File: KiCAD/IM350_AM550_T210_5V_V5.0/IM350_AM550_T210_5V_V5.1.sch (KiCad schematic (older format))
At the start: 32 parts, among them J1 USB_B_Micro_Power, J2 RJ12, Q1 BC847, SW1 SW_Push, U1 AMS1117-3.3, U2 ESP-12F, U3 TSS721ADR, U4 EL357NC, U5 EL357NC

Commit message: Update
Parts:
- removed R13: 0, Resistor_SMD:R_0201_0603Metric_Pad0.64x0.40mm_HandSolder, symbol Device:R
- added D1: 1N4148WS, Diode_SMD:D_SOD-323_HandSoldering, symbol Diode:1N4148WS
- U3: symbol TSS721ADR:TSS721ADR -> IM350_AM550_T210_5V_V5.0-rescue:TSS721ADR-TSS721ADR
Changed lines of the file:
@@
 NoConn ~ 1150 5400
 $Comp
-L TSS721ADR:TSS721ADR U3
+L IM350_AM550_T210_5V_V5.0-rescue:TSS721ADR-TSS721ADR U3
 U 1 1 61633360
 P 8200 2350
@@
 	8900 1650 9550 1650
 Wire Wire Line
-	7500 950  9550 950
-Wire Wire Line
 	2800 4600 2800 4650
 $Comp
@@
 Wire Wire Line
 	10250 2150 10250 2500
-$Comp
-L Device:R R13
-U 1 1 616AFA1A
-P 10150 2350
-F 0 "R13" V 10100 2500 50  0000 C CNN
-F 1 "0" V 10150 2350 50  0000 C CNN
-F 2 "Resistor_SMD:R_0201_0603Metric_Pad0.64x0.40mm_HandSolder" V 10080 2350 50  0001 C CNN
-F 3 "~" H 10150 2350 50  0001 C CNN
-	1    10150 2350
-	-1   0    0    1
-$EndComp
 Connection ~ 10250 2500
 Wire Wire Line
@@
 Text Label 2650 4400 0    50   ~ 0
 MBUS_RX
+$Comp
+L Diode:1N4148WS D1
+U 1 1 61830095
+P 10150 2350
+F 0 "D1" V 10250 2250 50  0000 L CNN
+F 1 "1N4148WS" V 10350 2150 50  0000 L CNN
+F 2 "Diode_SMD:D_SOD-323_HandSoldering" H 10150 2175 50  0001 C CNN
+F 3 "https://www.vishay.com/docs/85751/1n4148ws.pdf" H 10150 2350 50  0001 C CNN
+	1    10150 2350
+	0    1    1    0
+$EndComp
+Wire Wire Line
+	7500 950  9550 950
 $EndSCHEMATC

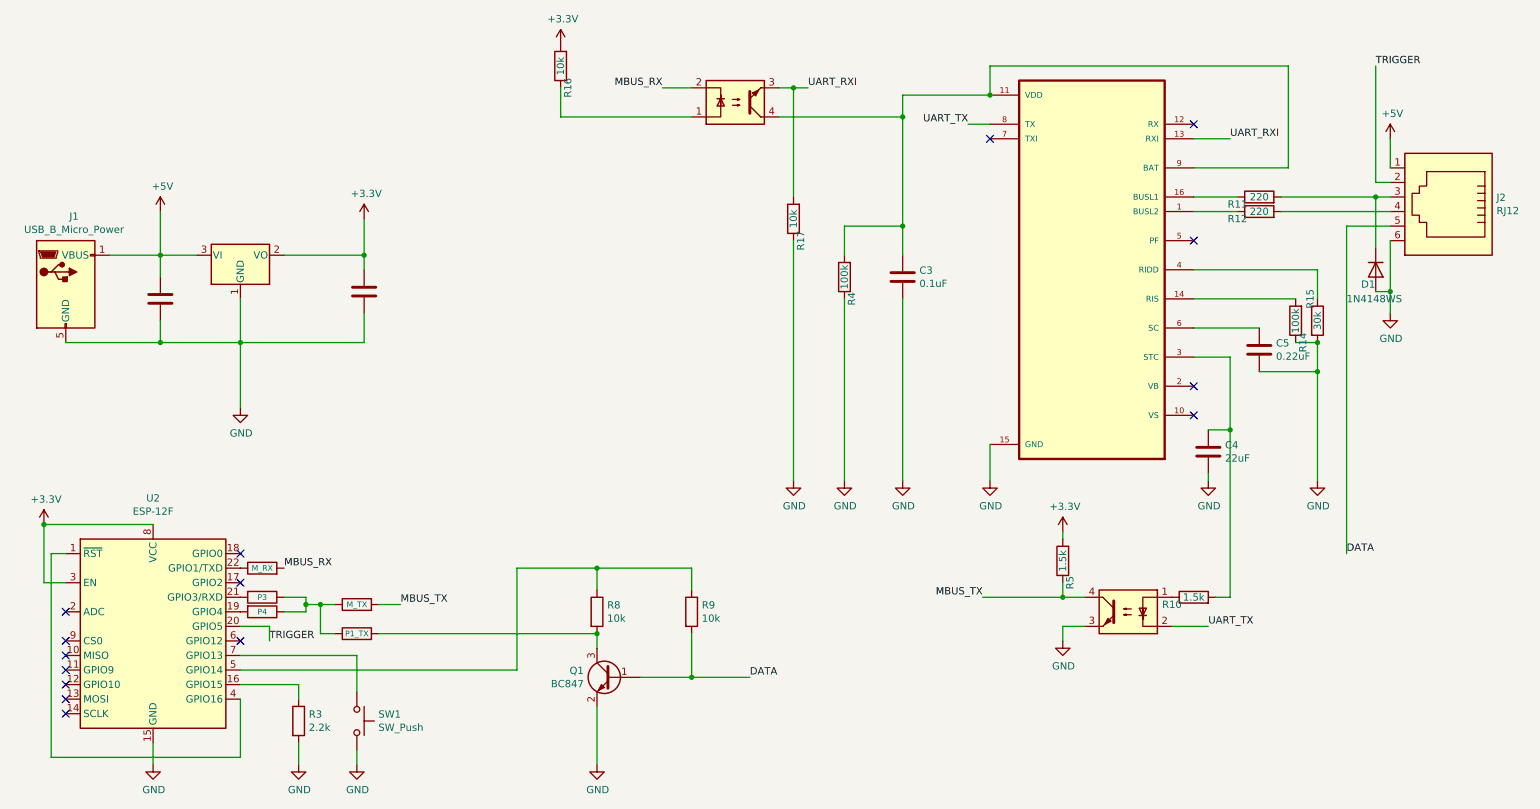
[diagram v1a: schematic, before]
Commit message: MBus for Smartmeter added
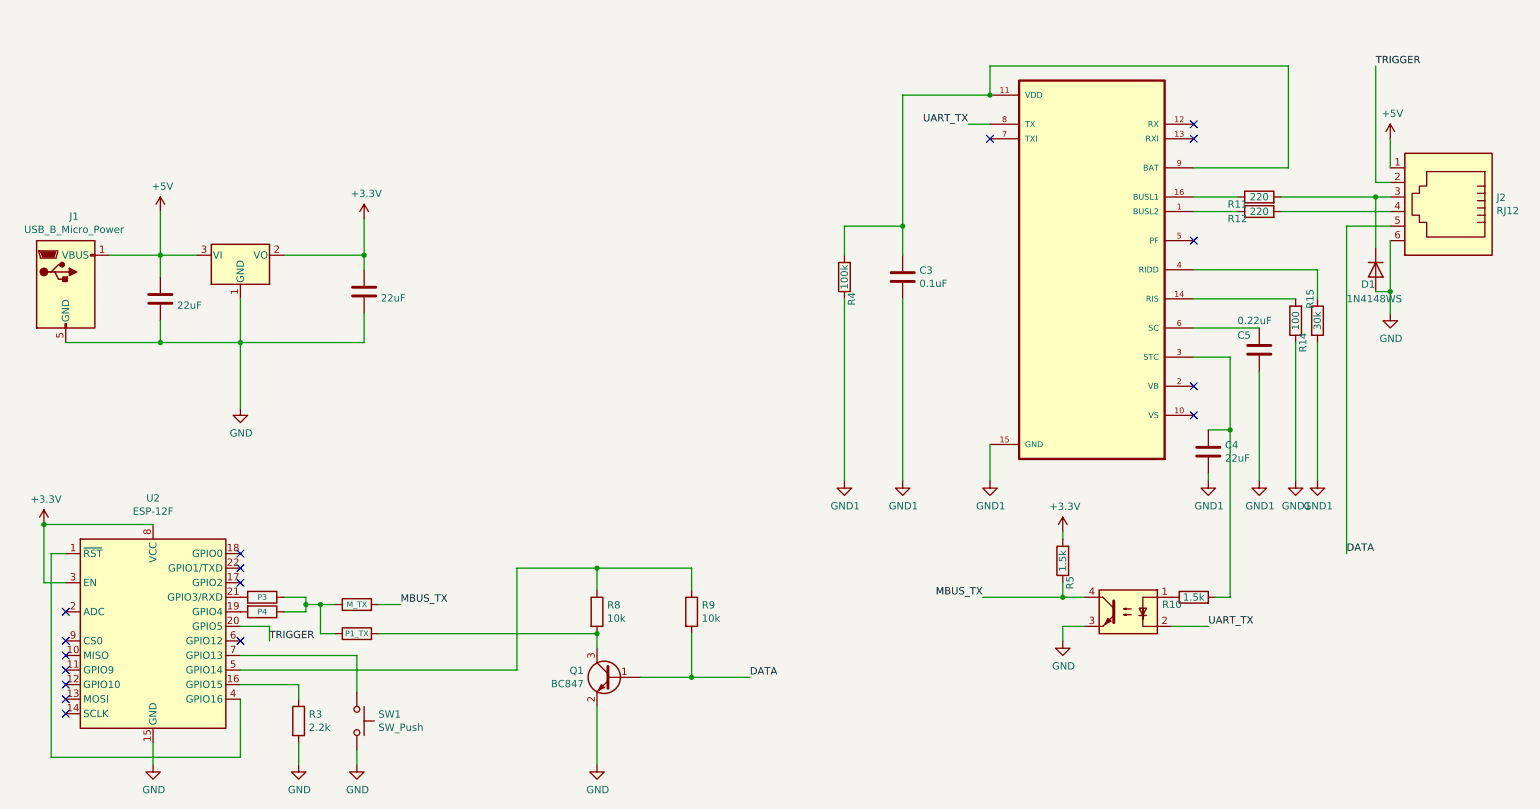
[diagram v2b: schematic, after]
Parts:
- removed R16, R17: 10k, Resistor_SMD:R_0805_2012Metric_Pad1.20x1.40mm_HandSolder, symbol Device:R
- removed R18: M_RX, Resistor_SMD:R_0201_0603Metric_Pad0.64x0.40mm_HandSolder, symbol Device:R
- removed U5: EL357NC, Package_SO:SOIC-4_4.55x2.6mm_P1.27mm, symbol Isolator:TLP291
- R1, R2, R6, R7: footprint Resistor_SMD:R_0201_0603Metric_Pad0.64x0.40mm_HandSolder -> Resistor_SMD:R_0603_1608Metric_Pad0.98x0.95mm_HandSolder
- R14: value 100k -> 100
- U4: footprint Package_SO:SOIC-4_4.55x2.6mm_P1.27mm -> Package_SO:SOP-4_3.8x4.1mm_P2.54mm
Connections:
- net GND: no longer C3.2, C4.2, C5.2, R14.1, R15.2, R4.1, U3.15 (GND)
- net UART_RXI: no longer names the net of U3.13 (RXI)
- new net GND1: C3.2, C4.2, C5.2, R14.1, R15.2, R4.1, U3.15 (GND)
- no-connect marks 15 -> 17
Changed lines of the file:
@@
 P 3200 2500
 F 0 "C1" H 3315 2546 50  0001 L CNN
-F 1 "22uF" H 3315 2455 50  0001 L CNN
+F 1 "22uF" H 3315 2455 50  0000 L CNN
 F 2 "Capacitor_SMD:C_1206_3216Metric_Pad1.33x1.80mm_HandSolder" H 3238 2350 50  0001 C CNN
 F 3 "~" H 3200 2500 50  0001 C CNN
@@
 F 0 "R1" V 2450 4750 50  0001 C CNN
 F 1 "P3" V 2500 4600 39  0000 C CNN
-F 2 "Resistor_SMD:R_0201_0603Metric_Pad0.64x0.40mm_HandSolder" V 2430 4600 50  0001 C CNN
+F 2 "Resistor_SMD:R_0603_1608Metric_Pad0.98x0.95mm_HandSolder" V 2430 4600 50  0001 C CNN
 F 3 "~" H 2500 4600 50  0001 C CNN
 	1    2500 4600
@@
 F 0 "R2" V 2550 4850 50  0001 C CNN
 F 1 "P4" V 2500 4700 39  0000 C CNN
-F 2 "Resistor_SMD:R_0201_0603Metric_Pad0.64x0.40mm_HandSolder" V 2430 4700 50  0001 C CNN
+F 2 "Resistor_SMD:R_0603_1608Metric_Pad0.98x0.95mm_HandSolder" V 2430 4700 50  0001 C CNN
 F 3 "~" H 2500 4700 50  0001 C CNN
 	1    2500 4700
@@
 Wire Wire Line
 	7500 3800 7500 3550
-$Comp
-L power:GND #PWR0102
-U 1 1 6164BD9D
-P 7500 3800
-F 0 "#PWR0102" H 7500 3550 50  0001 C CNN
-F 1 "GND" H 7505 3627 50  0000 C CNN
-F 2 "" H 7500 3800 50  0001 C CNN
-F 3 "" H 7500 3800 50  0001 C CNN
-	1    7500 3800
-	1    0    0    -1
-$EndComp
 NoConn ~ 7500 1450
 NoConn ~ 8900 2150
@@
 P 1800 2550
 F 0 "C2" H 1915 2596 50  0001 L CNN
-F 1 "22uF" H 1915 2505 50  0001 L CNN
+F 1 "22uF" H 1915 2505 50  0000 L CNN
 F 2 "Capacitor_SMD:C_1206_3216Metric_Pad1.33x1.80mm_HandSolder" H 1838 2400 50  0001 C CNN
 F 3 "~" H 1800 2550 50  0001 C CNN
@@
 F 0 "R6" V 3100 4800 50  0001 C CNN
 F 1 "M_TX" V 3150 4650 39  0000 C CNN
-F 2 "Resistor_SMD:R_0201_0603Metric_Pad0.64x0.40mm_HandSolder" V 3080 4650 50  0001 C CNN
+F 2 "Resistor_SMD:R_0603_1608Metric_Pad0.98x0.95mm_HandSolder" V 3080 4650 50  0001 C CNN
 F 3 "~" H 3150 4650 50  0001 C CNN
 	1    3150 4650
@@
 F 0 "R7" V 3100 5000 50  0001 C CNN
 F 1 "P1_TX" V 3150 4850 39  0000 C CNN
-F 2 "Resistor_SMD:R_0201_0603Metric_Pad0.64x0.40mm_HandSolder" V 3080 4850 50  0001 C CNN
+F 2 "Resistor_SMD:R_0603_1608Metric_Pad0.98x0.95mm_HandSolder" V 3080 4850 50  0001 C CNN
 F 3 "~" H 3150 4850 50  0001 C CNN
 	1    3150 4850
@@
 F 0 "U4" H 8450 5025 50  0001 C CNN
 F 1 "EL357NC" H 8450 4934 50  0001 C CNN
-F 2 "Package_SO:SOIC-4_4.55x2.6mm_P1.27mm" H 8250 4500 50  0001 L CNN
+F 2 "Package_SO:SOP-4_3.8x4.1mm_P2.54mm" H 8250 4500 50  0001 L CNN
 F 3 "https://toshiba.semicon-storage.com/info/docget.jsp?did=12884&prodName=TLP291" H 8450 4700 50  0001 L CNN
 	1    8450 4700
@@
 Wire Wire Line
 	7500 1150 6900 1150
-Wire Wire Line
-	6900 1150 6900 1300
 Connection ~ 7500 1150
-$Comp
-L power:GND #PWR02
-U 1 1 616F92D3
-P 6900 3800
-F 0 "#PWR02" H 6900 3550 50  0001 C CNN
-F 1 "GND" H 6905 3627 50  0000 C CNN
-F 2 "" H 6900 3800 50  0001 C CNN
-F 3 "" H 6900 3800 50  0001 C CNN
-	1    6900 3800
-	1    0    0    -1
-$EndComp
 Wire Wire Line
 	6900 2550 6900 3800
@@
 Wire Wire Line
 	6900 2050 6900 2250
-$Comp
-L power:GND #PWR01
-U 1 1 616FD0E7
-P 6500 3800
-F 0 "#PWR01" H 6500 3550 50  0001 C CNN
-F 1 "GND" H 6505 3627 50  0000 C CNN
-F 2 "" H 6500 3800 50  0001 C CNN
-F 3 "" H 6500 3800 50  0001 C CNN
-	1    6500 3800
-	1    0    0    -1
-$EndComp
 Wire Wire Line
 	6500 2550 6500 3800
@@
 P 9600 2700
 F 0 "R14" V 9550 2850 50  0000 C CNN
-F 1 "100k" V 9600 2700 50  0000 C CNN
+F 1 "100" V 9600 2700 50  0000 C CNN
 F 2 "Resistor_SMD:R_0805_2012Metric_Pad1.20x1.40mm_HandSolder" V 9530 2700 50  0001 C CNN
 F 3 "~" H 9600 2700 50  0001 C CNN
 	1    9600 2700
 	-1   0    0    1
-$EndComp
-$Comp
-L power:GND #PWR06
-U 1 1 6170140B
-P 9750 3800
-F 0 "#PWR06" H 9750 3550 50  0001 C CNN
-F 1 "GND" H 9755 3627 50  0000 C CNN
-F 2 "" H 9750 3800 50  0001 C CNN
-F 3 "" H 9750 3800 50  0001 C CNN
-	1    9750 3800
-	1    0    0    -1
 $EndComp
 $Comp
@@
 	8900 2950 9150 2950
 Wire Wire Line
-	9750 2850 9750 3050
-Wire Wire Line
 	9000 3450 9150 3450
 Connection ~ 9150 3450
 Wire Wire Line
 	9150 3450 9150 4600
-$Comp
-L power:GND #PWR05
-U 1 1 6173CE86
-P 9000 3800
-F 0 "#PWR05" H 9000 3550 50  0001 C CNN
-F 1 "GND" H 9005 3627 50  0000 C CNN
-F 2 "" H 9000 3800 50  0001 C CNN
-F 3 "" H 9000 3800 50  0001 C CNN
-	1    9000 3800
-	1    0    0    -1
-$EndComp
 Wire Wire Line
 	9000 3750 9000 3800
@@
 	1    0    0    -1
 $EndComp
-Wire Wire Line
-	9600 2850 9750 2850
-Connection ~ 9750 2850
 Wire Wire Line
 	9750 2350 9750 2550
@@
 U 1 1 61763C16
 P 9350 2900
-F 0 "C5" H 9465 2946 50  0000 L CNN
-F 1 "0.22uF" H 9465 2855 50  0000 L CNN
+F 0 "C5" H 9200 3000 50  0000 L CNN
+F 1 "0.22uF" H 9200 3100 50  0000 L CNN
 F 2 "Capacitor_SMD:C_1206_3216Metric_Pad1.33x1.80mm_HandSolder" H 9388 2750 50  0001 C CNN
 F 3 "~" H 9350 2900 50  0001 C CNN
@@
 Wire Wire Line
 	8900 2750 9350 2750
-Wire Wire Line
-	9350 3050 9750 3050
-Connection ~ 9750 3050
-Wire Wire Line
-	9750 3050 9750 3800
-$Comp
-L Isolator:TLP291 U5
-U 1 1 6176F157
-P 5750 1200
-F 0 "U5" H 5750 883 50  0001 C CNN
-F 1 "EL357NC" H 5750 974 50  0001 C CNN
-F 2 "Package_SO:SOIC-4_4.55x2.6mm_P1.27mm" H 5550 1000 50  0001 L CIN
-F 3 "https://toshiba.semicon-storage.com/info/docget.jsp?did=12884&prodName=TLP291" H 5750 1200 50  0001 L CNN
-	1    5750 1200
-	1    0    0    1
-$EndComp
-Wire Wire Line
-	6050 1300 6900 1300
-Connection ~ 6900 1300
-Wire Wire Line
-	6900 1300 6900 2050
-Text Label 9150 1450 0    50   ~ 0
-UART_RXI
-Wire Wire Line
-	8900 1450 9150 1450
-Text Label 6250 1100 0    50   ~ 0
-UART_RXI
-Wire Wire Line
-	6050 1100 6150 1100
-Text Label 5250 1100 2    50   ~ 0
-MBUS_RX
-Wire Wire Line
-	5250 1100 5450 1100
-$Comp
-L Device:R R17
-U 1 1 61789B8F
-P 6150 2000
-F 0 "R17" V 6100 2150 50  0000 C CNN
-F 1 "10k" V 6150 2000 50  0000 C CNN
-F 2 "Resistor_SMD:R_0805_2012Metric_Pad1.20x1.40mm_HandSolder" V 6080 2000 50  0001 C CNN
-F 3 "~" H 6150 2000 50  0001 C CNN
-	1    6150 2000
-	-1   0    0    1
-$EndComp
-Wire Wire Line
-	6150 1100 6150 1850
-Connection ~ 6150 1100
-Wire Wire Line
-	6150 1100 6250 1100
-$Comp
-L power:GND #PWR08
-U 1 1 6178CDD3
-P 6150 3800
-F 0 "#PWR08" H 6150 3550 50  0001 C CNN
-F 1 "GND" H 6155 3627 50  0000 C CNN
-F 2 "" H 6150 3800 50  0001 C CNN
-F 3 "" H 6150 3800 50  0001 C CNN
-	1    6150 3800
-	1    0    0    -1
-$EndComp
-Wire Wire Line
-	6150 2150 6150 3800
-$Comp
-L Device:R R16
-U 1 1 61790C22
-P 4550 950
-F 0 "R16" V 4500 1100 50  0000 C CNN
-F 1 "10k" V 4550 950 50  0000 C CNN
-F 2 "Resistor_SMD:R_0805_2012Metric_Pad1.20x1.40mm_HandSolder" V 4480 950 50  0001 C CNN
-F 3 "~" H 4550 950 50  0001 C CNN
-	1    4550 950
-	-1   0    0    1
-$EndComp
-Wire Wire Line
-	5450 1300 4550 1300
-Wire Wire Line
-	4550 1300 4550 1100
-$Comp
-L power:+3.3V #PWR07
-U 1 1 61794900
-P 4550 800
-F 0 "#PWR07" H 4550 650 50  0001 C CNN
-F 1 "+3.3V" H 4565 973 50  0000 C CNN
-F 2 "" H 4550 800 50  0001 C CNN
-F 3 "" H 4550 800 50  0001 C CNN
-	1    4550 800
-	1    0    0    -1
-$EndComp
 NoConn ~ 8900 1350
-$Comp
-L Device:R R18
-U 1 1 61798BED
-P 2500 4400
-F 0 "R18" V 2450 4550 50  0001 C CNN
-F 1 "M_RX" V 2500 4400 39  0000 C CNN
-F 2 "Resistor_SMD:R_0201_0603Metric_Pad0.64x0.40mm_HandSolder" V 2430 4400 50  0001 C CNN
-F 3 "~" H 2500 4400 50  0001 C CNN
-	1    2500 4400
-	0    -1   -1   0
-$EndComp
-Text Label 2650 4400 0    50   ~ 0
-MBUS_RX
 $Comp
 L Diode:1N4148WS D1
@@
 $EndComp
 Wire Wire Line
+	9750 2850 9750 3800
+Wire Wire Line
+	9350 3050 9350 3800
+Wire Wire Line
+	9600 2850 9600 3800
+$Comp
+L power:GND1 #PWR02
+U 1 1 61C615B2
+P 6500 3800
+F 0 "#PWR02" H 6500 3550 50  0001 C CNN
+F 1 "GND1" H 6505 3627 50  0000 C CNN
+F 2 "" H 6500 3800 50  0001 C CNN
+F 3 "" H 6500 3800 50  0001 C CNN
+	1    6500 3800
+	1    0    0    -1
+$EndComp
+$Comp
+L power:GND1 #PWR05
+U 1 1 61C617FA
+P 6900 3800
+F 0 "#PWR05" H 6900 3550 50  0001 C CNN
+F 1 "GND1" H 6905 3627 50  0000 C CNN
+F 2 "" H 6900 3800 50  0001 C CNN
+F 3 "" H 6900 3800 50  0001 C CNN
+	1    6900 3800
+	1    0    0    -1
+$EndComp
+$Comp
+L power:GND1 #PWR06
+U 1 1 61C61A35
+P 7500 3800
+F 0 "#PWR06" H 7500 3550 50  0001 C CNN
+F 1 "GND1" H 7505 3627 50  0000 C CNN
+F 2 "" H 7500 3800 50  0001 C CNN
+F 3 "" H 7500 3800 50  0001 C CNN
+	1    7500 3800
+	1    0    0    -1
+$EndComp
+$Comp
+L power:GND1 #PWR08
+U 1 1 61C61C0B
+P 9000 3800
+F 0 "#PWR08" H 9000 3550 50  0001 C CNN
+F 1 "GND1" H 9005 3627 50  0000 C CNN
+F 2 "" H 9000 3800 50  0001 C CNN
+F 3 "" H 9000 3800 50  0001 C CNN
+	1    9000 3800
+	1    0    0    -1
+$EndComp
+$Comp
+L power:GND1 #PWR09
+U 1 1 61C61F24
+P 9350 3800
+F 0 "#PWR09" H 9350 3550 50  0001 C CNN
+F 1 "GND1" H 9355 3627 50  0000 C CNN
+F 2 "" H 9350 3800 50  0001 C CNN
+F 3 "" H 9350 3800 50  0001 C CNN
+	1    9350 3800
+	1    0    0    -1
+$EndComp
+$Comp
+L power:GND1 #PWR010
+U 1 1 61C62151
+P 9600 3800
+F 0 "#PWR010" H 9600 3550 50  0001 C CNN
+F 1 "GND1" H 9605 3627 50  0000 C CNN
+F 2 "" H 9600 3800 50  0001 C CNN
+F 3 "" H 9600 3800 50  0001 C CNN
+	1    9600 3800
+	1    0    0    -1
+$EndComp
+$Comp
+L power:GND1 #PWR011
+U 1 1 61C6227B
+P 9750 3800
+F 0 "#PWR011" H 9750 3550 50  0001 C CNN
+F 1 "GND1" H 9755 3627 50  0000 C CNN
+F 2 "" H 9750 3800 50  0001 C CNN
+F 3 "" H 9750 3800 50  0001 C CNN
+	1    9750 3800
+	1    0    0    -1
+$EndComp
+Wire Wire Line
 	7500 950  9550 950
+NoConn ~ 8900 1450
+Wire Wire Line
+	6900 1150 6900 2050
+NoConn ~ 2350 4400
 $EndSCHEMATC
